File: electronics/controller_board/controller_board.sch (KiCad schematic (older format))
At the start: 58 parts

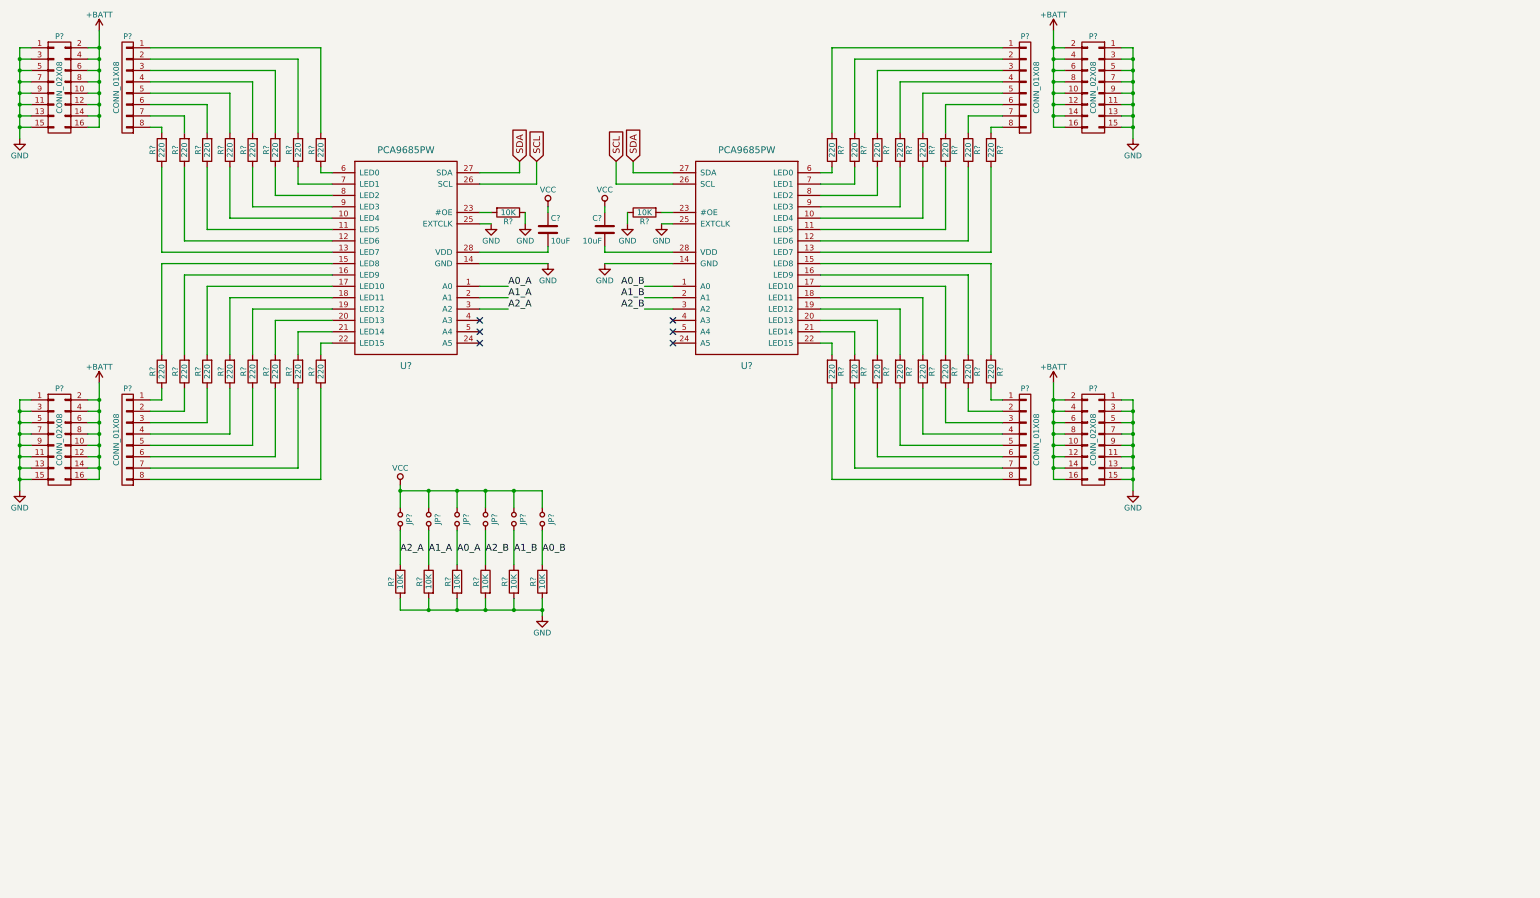
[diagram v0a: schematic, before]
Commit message: add bno055 in controller board
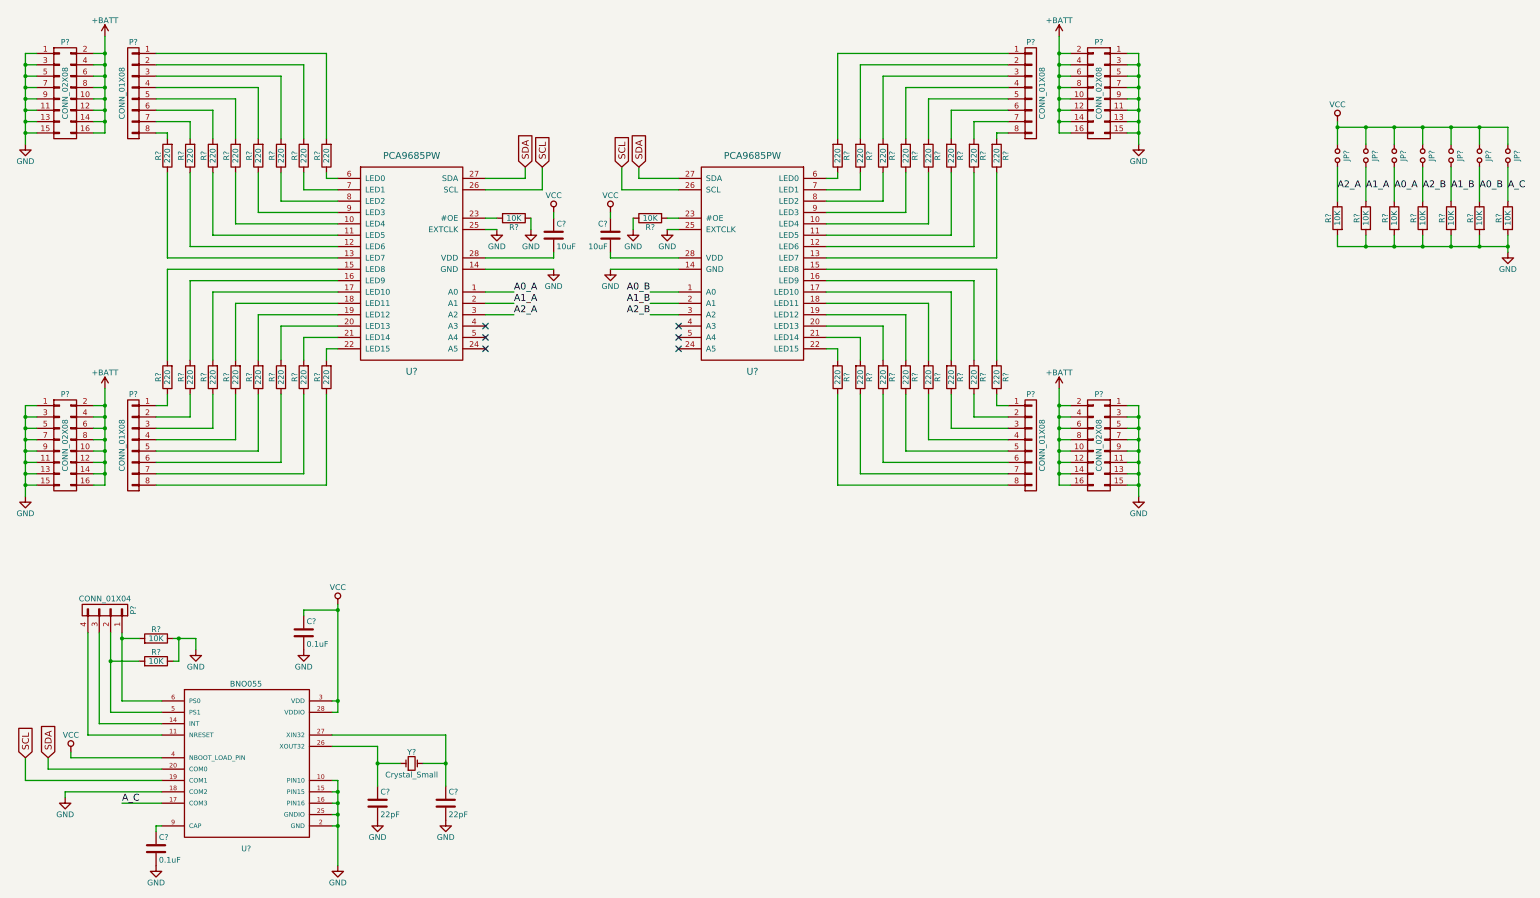
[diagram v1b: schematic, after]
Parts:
- added C? (x2): 0.1uF, symbol C
- added C? (x2): 22pF, symbol C
- added JP?: Jumper_NO_Small, symbol Jumper_NO_Small
- added P?: CONN_01X04, symbol CONN_01X04
- added R? (x3): 10K, symbol R
- added U?: BNO055, , symbol BNO055
- added Y?: Crystal_Small, symbol Crystal_Small
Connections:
- net GND: now also C?.2, C?.2, C?.2, C?.2, R?.1, R?.1, R?.2, U?.10 (PIN10), U?.15 (PIN15), U?.16 (PIN16), U?.18 (COM2), U?.2 (GND), U?.25 (GNDIO)
- net SCL: now also U?.19 (COM1)
- net SDA: now also U?.20 (COM0)
- net VCC: now also C?.1, JP?.1, U?.28 (VDDIO), U?.3 (VDD), U?.4 (NBOOT_LOAD_PIN)
- new net: C?.1, U?.9 (CAP)
- new net: P?.2 (P2), R?.2, U?.5 (PS1)
- new net: P?.1 (P1), R?.2, U?.6 (PS0)
- new net: P?.4 (P4), U?.11 (NRESET)
- new net: P?.3 (P3), U?.14 (INT)
- new net: C?.1, U?.26 (XOUT32), Y?.1
- new net: C?.1, U?.27 (XIN32), Y?.2
- new net A_C: JP?.2, R?.1, U?.17 (COM3)
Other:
- moved on the sheet: C?, JP?, P?, R?, U?

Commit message: arietta socket, led, i2c pull up resistor...
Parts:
- added D?: LED, symbol LED
- added P?: Arietta G25, symbol CONN_02X20
- added P?: Arietta G25 aux, symbol CONN_02X20
- added R? (x2): 10K, symbol R
- added R?: 220, symbol R
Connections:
- net GND: now also P?.9 (P9), P?.9 (P9), R?.1
- net SCL: now also P?.12 (P12), P?.12 (P12), R?.2
- net SDA: now also P?.14 (P14), P?.14 (P14), R?.2
- net VCC: now also D?.2 (A), P?.5 (P5), P?.5 (P5), R?.1, R?.1
- new net: D?.1 (K), R?.2
- new net 1W: P?.35 (P35), P?.35 (P35)
- new net 5V: P?.1 (P1), P?.1 (P1)
- new net ADC2: P?.38 (P38), P?.38 (P38)
- new net ADC3: P?.40 (P40), P?.40 (P40)
- new net NSRT: P?.3 (P3), P?.3 (P3)
- new net PA24: P?.11 (P11), P?.11 (P11)
- new net PA25: P?.13 (P13), P?.13 (P13)
- new net PA26: P?.15 (P15), P?.15 (P15)
- new net PA27: P?.17 (P17), P?.17 (P17)
- new net PA28: P?.19 (P19), P?.19 (P19)
- new net PA29: P?.21 (P21), P?.21 (P21)
- new net PA7: P?.26 (P26), P?.26 (P26)
- new net PC0: P?.39 (P39), P?.39 (P39)
- new net PC1: P?.37 (P37), P?.37 (P37)
- new net PC27: P?.30 (P30), P?.30 (P30)
- new net PC28: P?.29 (P29), P?.29 (P29)
- new net PC3: P?.33 (P33), P?.33 (P33)
- new net PC31: P?.32 (P32), P?.32 (P32)
- new net PC4: P?.31 (P31), P?.31 (P31)
- new net PWM0: P?.34 (P34), P?.34 (P34)
- new net PWM1: P?.36 (P36), P?.36 (P36)
- new net RXD0: P?.24 (P24), P?.24 (P24)
- new net RXD1: P?.27 (P27), P?.27 (P27)
- new net SPI1_CK: P?.7 (P7), P?.7 (P7)
- new net SPI1_CS0: P?.25 (P25), P?.25 (P25)
- new net SPI1_MISO: P?.10 (P10), P?.10 (P10)
- new net SPI1_MOSI: P?.8 (P8), P?.8 (P8)
- new net TXD0: P?.23 (P23), P?.23 (P23)
- new net TXD1: P?.28 (P28), P?.28 (P28)
- new net USB_A_D+: P?.6 (P6), P?.6 (P6)
- new net USB_A_D-: P?.4 (P4), P?.4 (P4)
- new net USB_B_D+: P?.16 (P16), P?.16 (P16)
- new net USB_B_D-: P?.18 (P18), P?.18 (P18)
- new net USB_C_D+: P?.22 (P22), P?.22 (P22)
- new net USB_C_D-: P?.20 (P20), P?.20 (P20)
- new net VBAT: P?.2 (P2), P?.2 (P2)

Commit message: place some components on PCB
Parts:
- added C7, C8: 330uF, Capacitors_SMD:c_elec_10x10, symbol CP1
- added D2: MBRS340T3G, Diodes_SMD:DO-214AB_Handsoldering, symbol D_Schottky
- added L1: 47uH, Choke_SMD:Choke_SMD_12x12mm_h8mm, symbol INDUCTOR
- added P12: CONN_01X02, Pin_Headers:Pin_Header_Straight_1x02, symbol CONN_01X02
- added P13: USB_A, Connect:USB_A_Vertical, symbol USB_A
- added U4: AP1509, Housings_SOIC:SOIC-8_3.9x4.9mm_Pitch1.27mm, symbol AP1509
- C1, C2, C3, C4, C5, C6: renamed from C?; footprint (none) -> Capacitors_SMD:C_0603_HandSoldering
- D1: renamed from D?; footprint (none) -> LEDs:LED_0603
- JP1, JP2, JP3, JP4, JP5, JP6, JP7: renamed from JP?; footprint (none) -> Capacitors_Tantalum_SMD:TantalC_SizeS_EIA-3216
- P1, P4, P5, P8: renamed from P?; footprint (none) -> Pin_Headers:Pin_Header_Straight_2x08
- P10, P11: renamed from P?; footprint (none) -> Pin_Headers:Pin_Header_Straight_2x20
- P2, P3, P6, P7: renamed from P?; footprint (none) -> Pin_Headers:Pin_Header_Straight_1x08
- P9: renamed from P?; footprint (none) -> Pin_Headers:Pin_Header_Straight_1x04
- R1, R10, R11, R12, R13, R14, R15, R16, R17, R18, R19, R2, R20, R21, R22, R23, R24, R25, R26, R27, R28, R29, R3, R30, R31, R32, R33, R34, R35, R36, R37, R38, R39, R4, R40, R41, R42, R43, R44, R45, R46, R5, R6, R7, R8, R9: renamed from R?; footprint (none) -> Resistors_SMD:R_0603_HandSoldering
- U1, U2: renamed from U?; footprint (none) -> Housings_SSOP:TSSOP-28_4.4x9.7mm_Pitch0.65mm
- U3: renamed from U?; footprint (none) -> Housings_DFN_QFN:DFN-18-1EP_4x5mm_Pitch0.5mm
- Y1: renamed from Y?; footprint (none) -> Crystals:Crystal_HC49-SD_SMD
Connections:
- net +BATT: now also C7.1, P12.1 (P1), U4.1 (VIN)
- net GND: now also C7.2, C8.2, D2.2 (A), P12.2 (P2), P13.4 (GND), U4.4 (SD), U4.5 (GND), U4.6 (GND), U4.7 (GND), U4.8 (GND)
- net USB_C_D+: now also P13.3 (D+)
- net USB_C_D-: now also P13.2 (D-)
- net VCC: now also C8.1, L1.2, P13.1 (VCC), P13.5 (shield), U4.3 (FB)
- new net: D2.1 (K), L1.1, U4.2 (Output)
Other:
- moved on the sheet: C3, C4, C5, C6, D1, JP1, JP2, JP3, JP4, JP5, JP6, JP7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

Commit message: More routing on board
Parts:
- removed P11: Arietta G25 aux, Pin_Headers:Pin_Header_Straight_2x20, symbol CONN_02X20
- U3: symbol BNO055 -> BNO055-RESCUE-controller_board
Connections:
- net GND: now also P13.5 (shield)
- net VCC: no longer P13.5 (shield)
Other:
- moved on the sheet: P10, P13
